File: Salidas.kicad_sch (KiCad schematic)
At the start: 0 parts

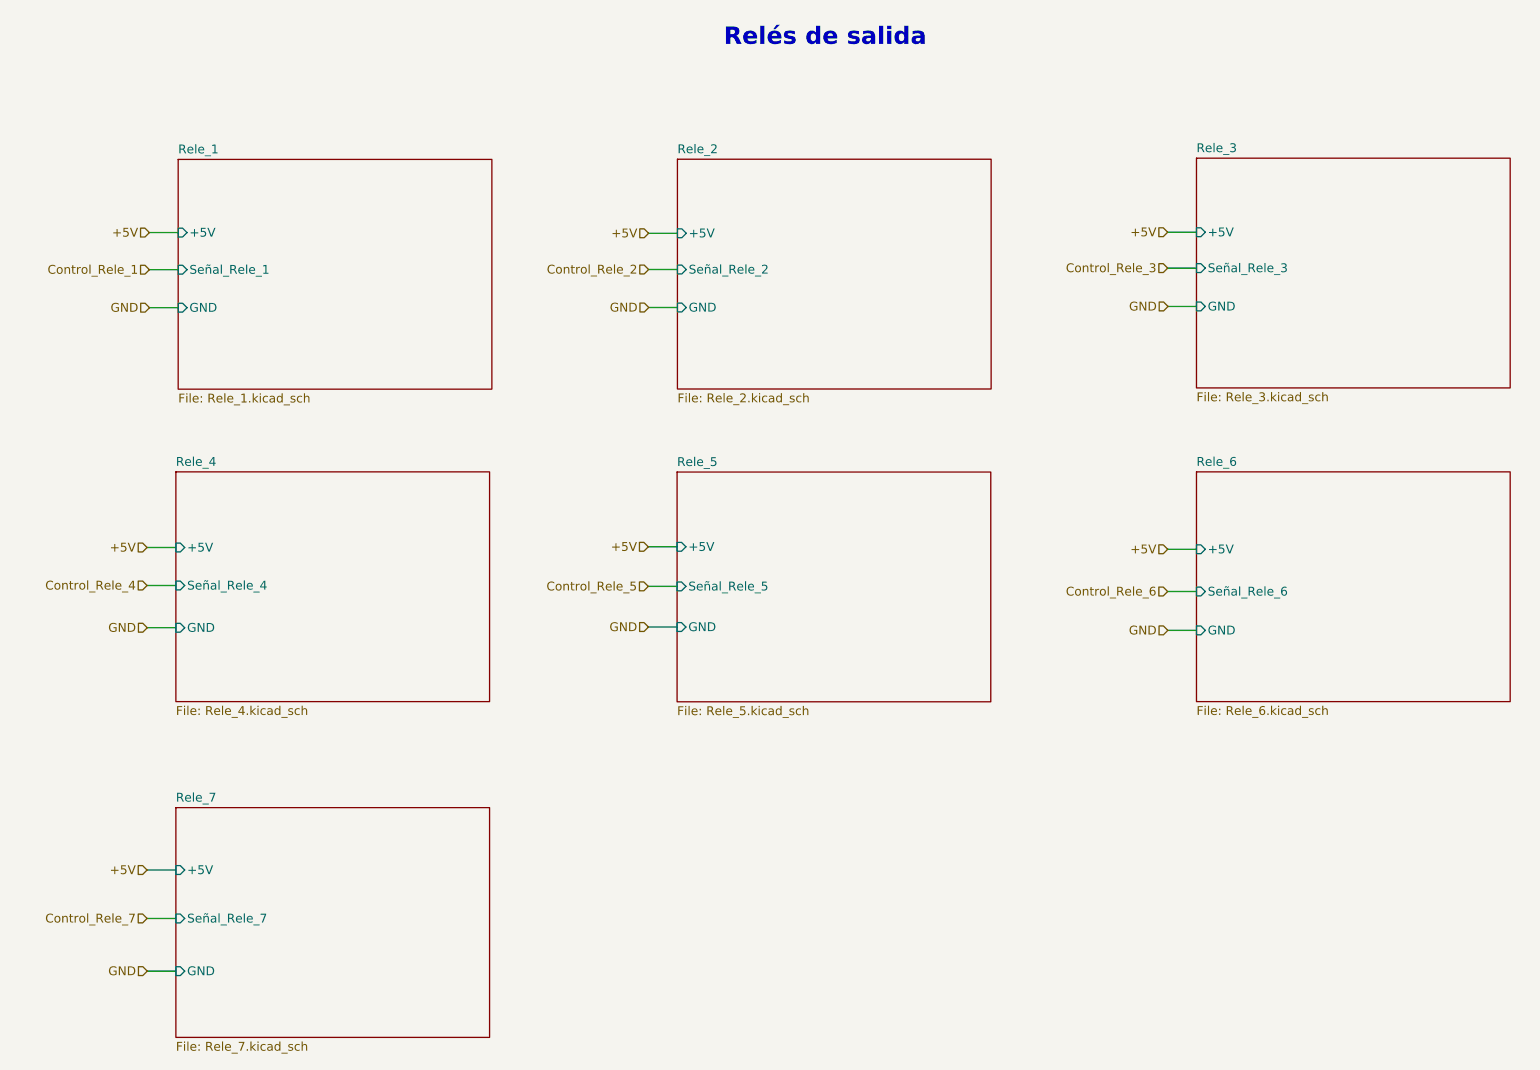
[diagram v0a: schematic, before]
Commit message: Actualización de SCH según placa industrial, y búsqueda de footprints.
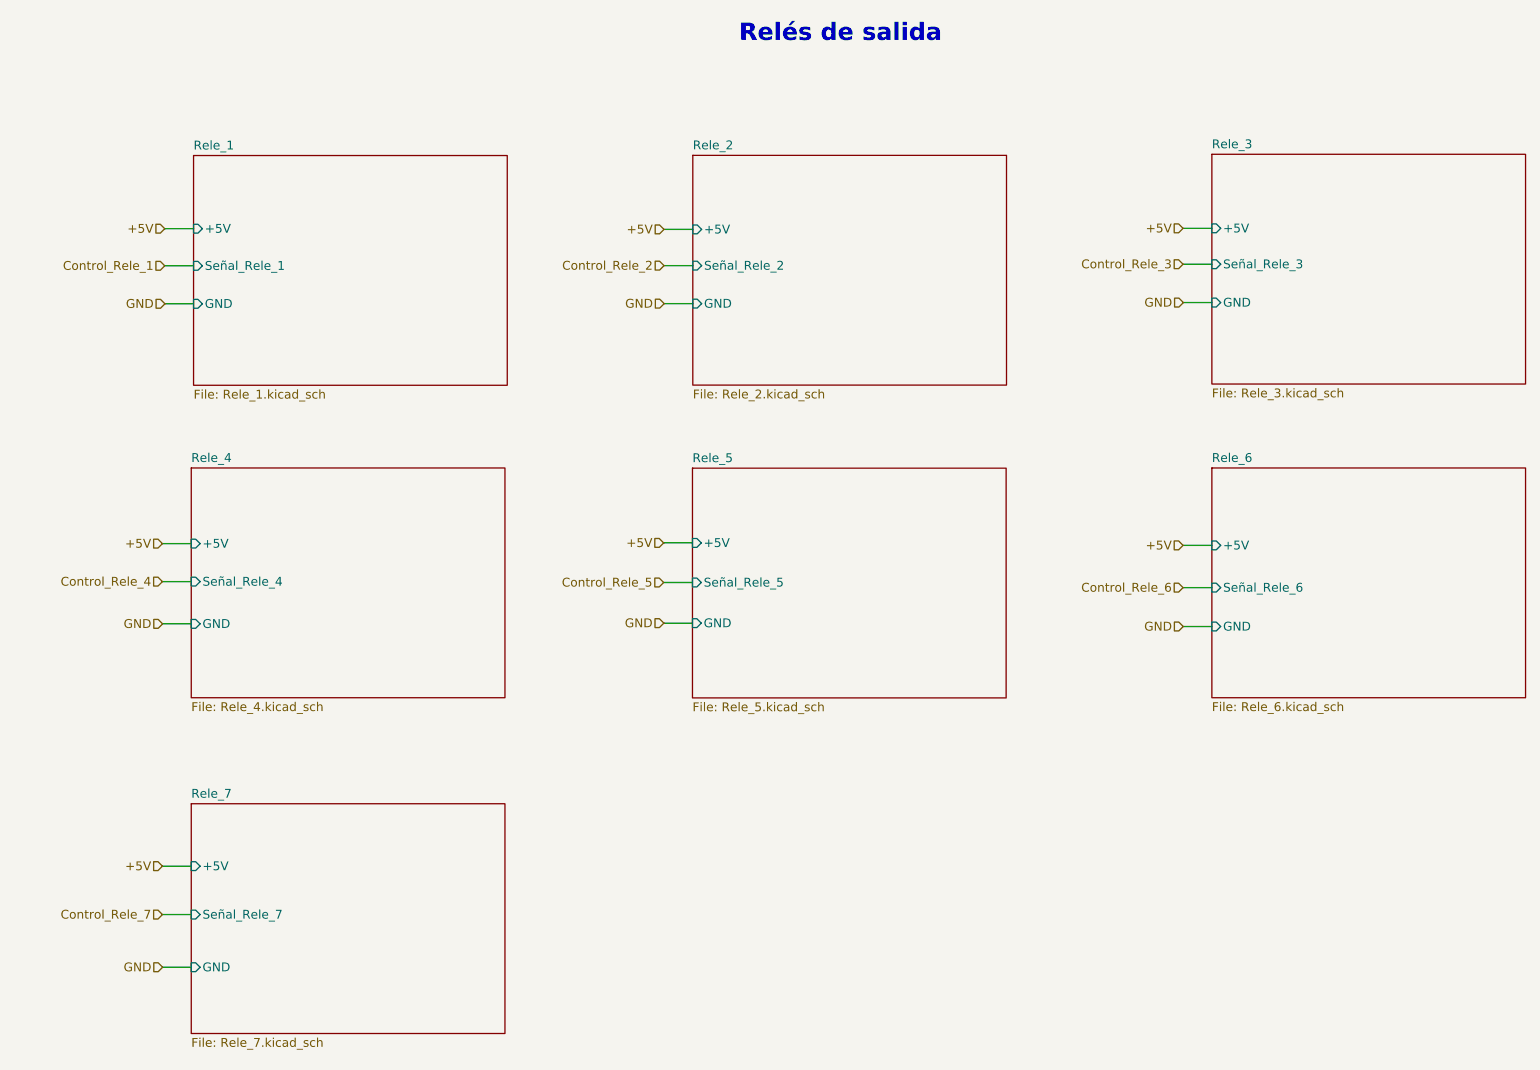
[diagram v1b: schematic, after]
